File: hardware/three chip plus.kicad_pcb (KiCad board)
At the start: 2 copper layers, 137.2 x 196.8 mm, 44 parts, among them J1 POWER, J2 PORT B, J3 PORT A, J4 Conn_01x10_Male, J5 ADDRESS BUS, J6 DATA BUS, J7 R/~W, SW1 RESET, U1 74LS14, U2 74LS32, U3 74LS08, U4 6522, U5 6502, U6 74LS138, U7 2716, U8 2114, U9 2114, X1 ACO-1MHz

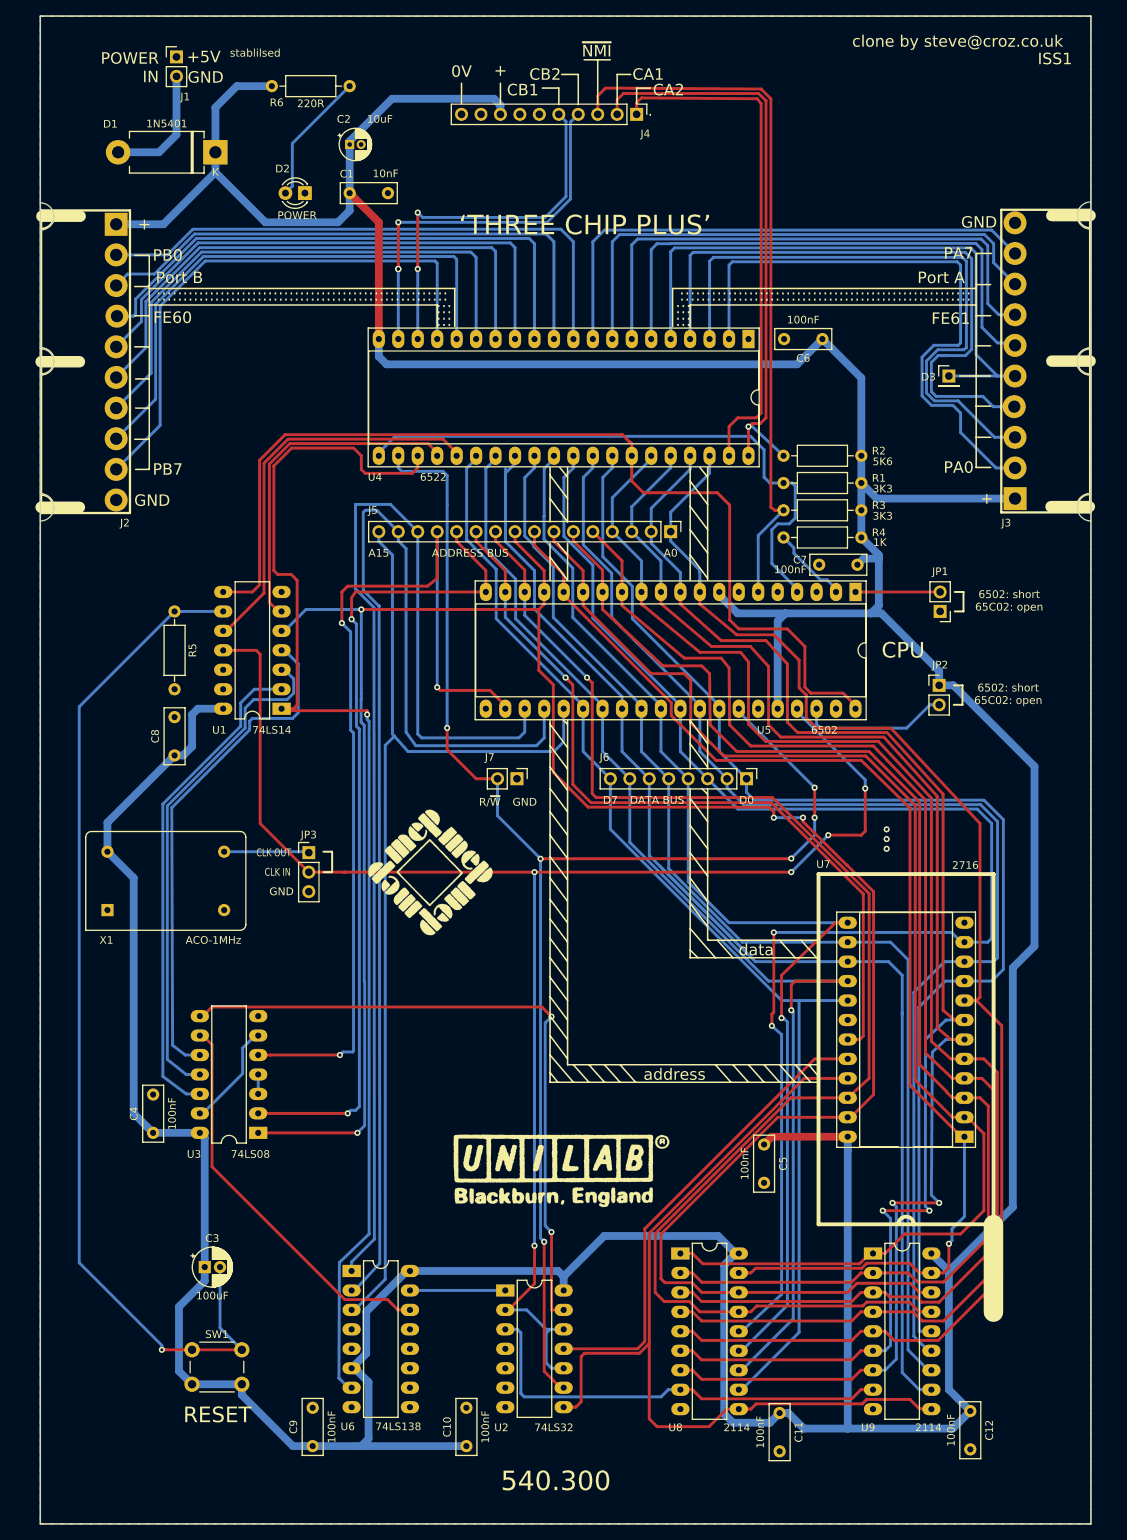
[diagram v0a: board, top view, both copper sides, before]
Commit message: ISS2 Updates
Change log:
1. corrected error in PHI2/~PHI2~ clocks to U4 and U2 (schematic & PCB)
2. made D1 parallel protection to avoid volt drop on +5V rail
3. added missing R5, C2 legends (PCB)
4. corrected Power In legend polarity (PCB)
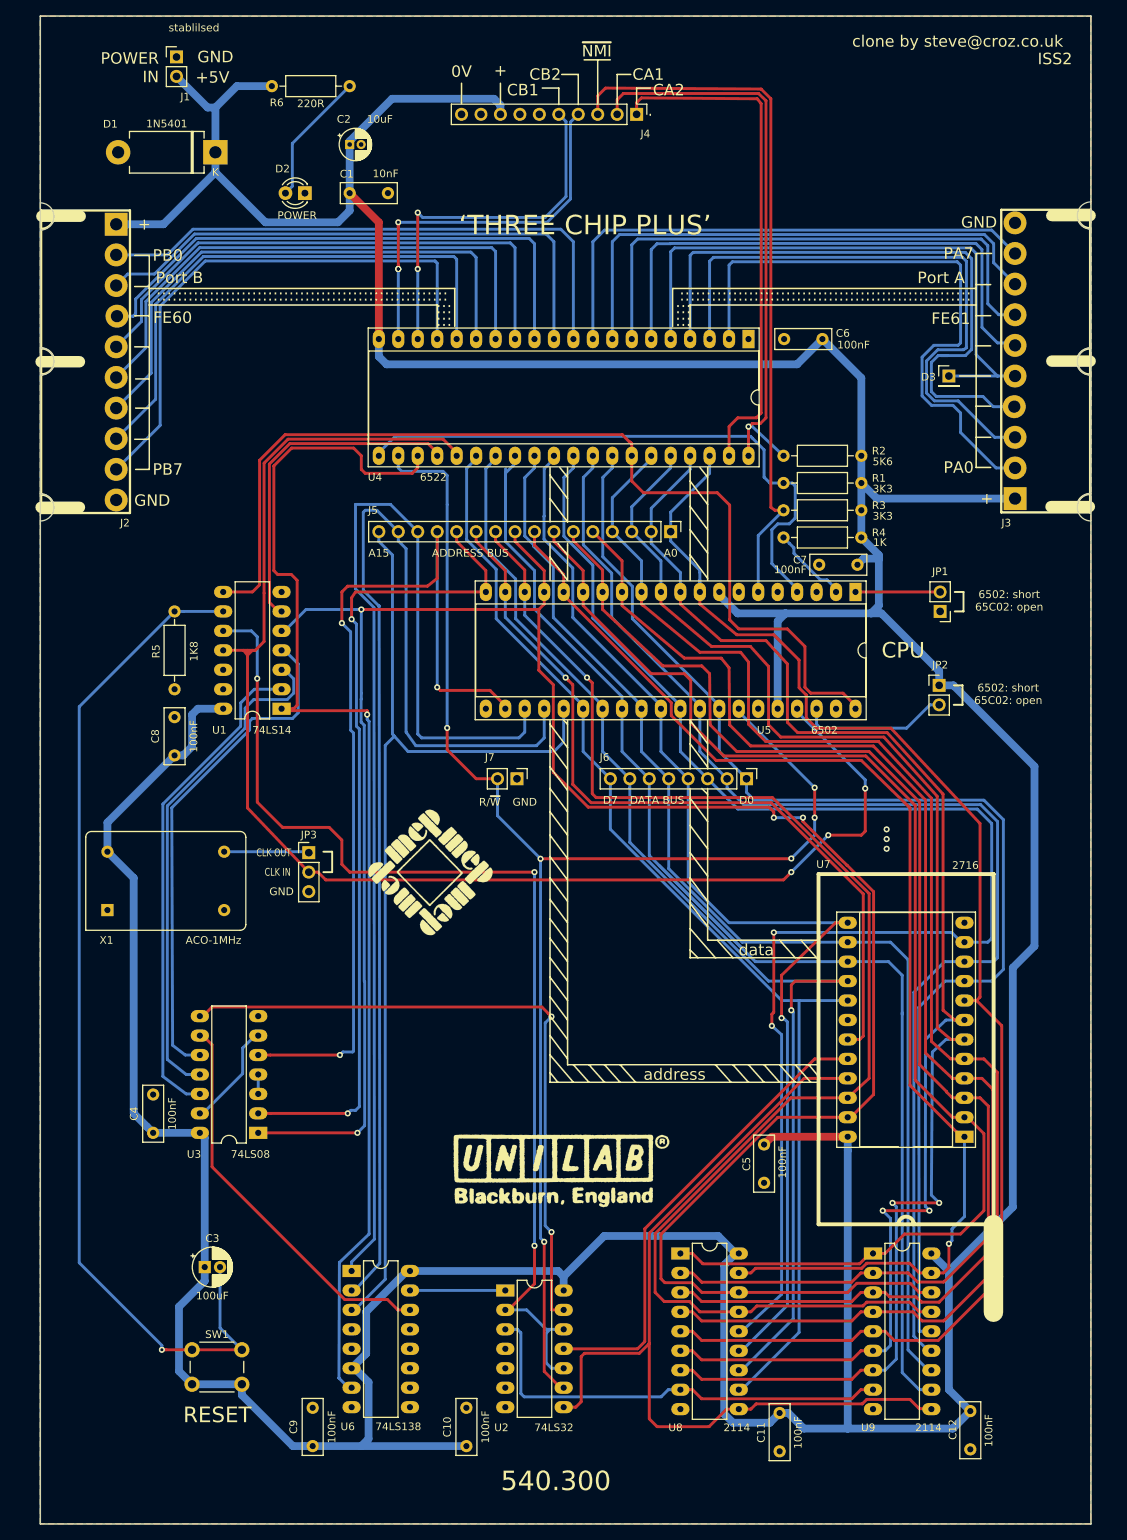
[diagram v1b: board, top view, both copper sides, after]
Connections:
- D1 pad 2: Net-(D1-Pad2) -> GND
- J1 pad 2: Net-(D1-Pad2) -> +5V
- JP3 pad 2: ~PHI2 -> Net-(JP3-Pad2)
- U1 pad 10: /PHI2 -> ~PHI2
- U1 pad 11: ~PHI2 -> Net-(JP3-Pad2)
- U4 pad 25: /PHI2 -> Net-(JP3-Pad2)
- U5 pad 37: ~PHI2 -> Net-(JP3-Pad2)
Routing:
- net Net-(JP3-Pad2): track 0.00 -> 185.6 mm, vias 0 -> 3
- net ~PHI2: track 205.7 -> 143.4 mm, vias 5 -> 3
- net /PHI2: track 51.9 -> 0.00 mm
- net Net-(D1-Pad2): track 16.2 -> 0.00 mm
- net +5V: track 720.0 -> 726.8 mm
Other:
- board text added: "ISS2"
- board text removed: "ISS1"
